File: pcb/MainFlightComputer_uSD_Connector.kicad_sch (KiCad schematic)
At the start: 10 parts, among them J5 0472192001

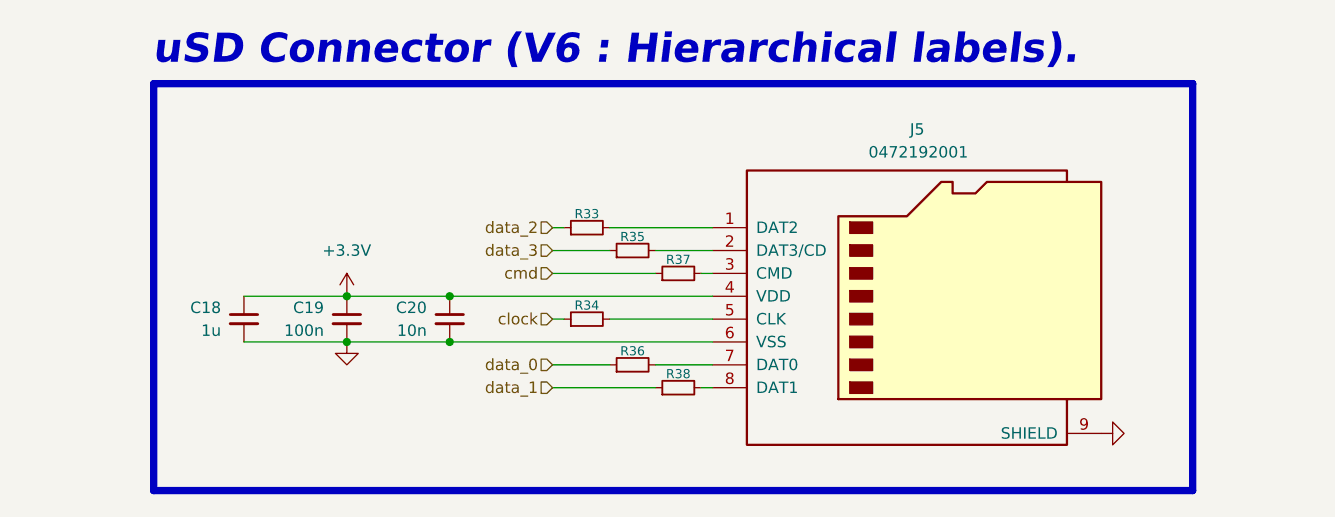
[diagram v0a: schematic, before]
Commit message: Updated design blocks in `MainFlightComputer`.
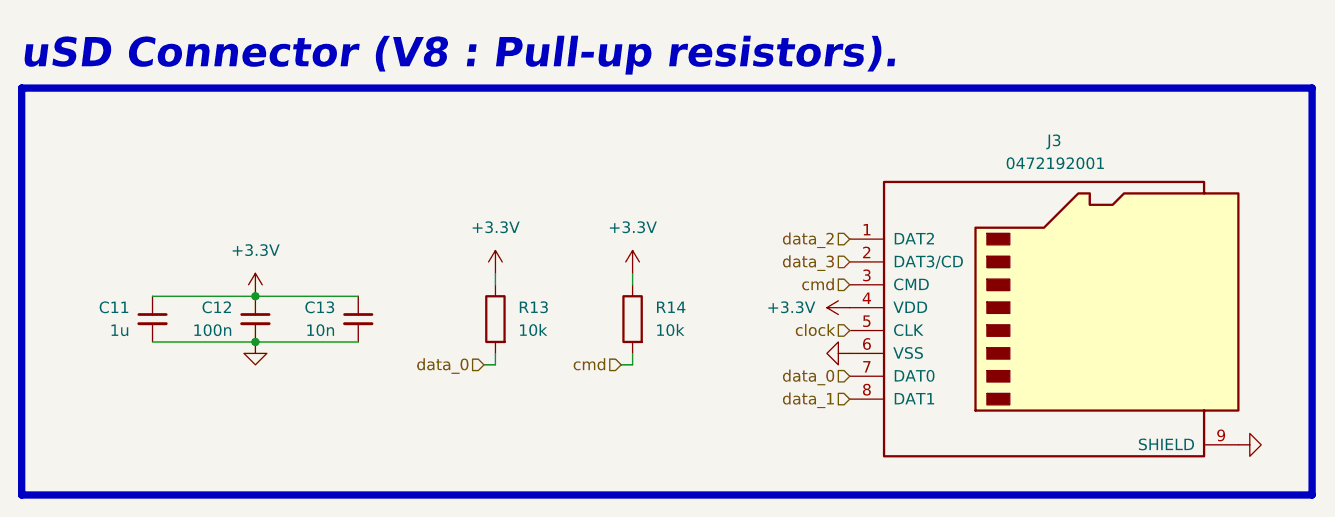
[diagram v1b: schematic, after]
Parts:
- removed R33, R34, R35, R36, R37, R38: R_Small, Resistor_SMD:R_1206_3216Metric_Pad1.30x1.75mm_HandSolder, symbol Device:R_Small
- added R13, R14: 10k, Resistor_SMD:R_1206_3216Metric_Pad1.30x1.75mm_HandSolder, symbol Device:R
- renumbered C18 to C11, C19 to C12, C20 to C13, J5 to J3
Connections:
- net +3.3V: now also R13.1, R14.1
- net clock: now also J3.5 (CLK)
- net cmd: now also J3.3 (CMD), R14.2
- net data_0: now also J3.7 (DAT0), R13.2
- net data_1: now also J3.8 (DAT1)
- net data_2: now also J3.1 (DAT2)
- net data_3: now also J3.2 (DAT3/CD)
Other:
- note added: "uSD Connector (V8 : Pull-up resistors)."
- note removed: "uSD Connector (V6 : Hierarchical labels)."
- moved on the sheet: C11, C12, C13, J3

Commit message: Laid out silkscreen for `MainFlightComputer`.
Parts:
- renumbered C13 to C17, C12 to C18, C11 to C19, J3 to J2, R13 to R14, R14 to R15
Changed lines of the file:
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@@
 		(on_board yes)
 		(dnp no)
-		(property "Reference" "R14"
+		(property "Reference" "R15"
 			(at 100.33 78.7399 0)
 			(effects
@@
 			(project ""
 				(path "/0a179c33-cb18-4019-99e7-0e00d41f97d6/d6d791b4-6a15-48a1-8b16-290665bcc58d"
-					(reference "R14")
+					(reference "R15")
 					(unit 1)
 				)
@@
 		(on_board yes)
 		(dnp no)
-		(property "Reference" "C11"
+		(property "Reference" "C19"
 			(at 41.91 78.7462 0)
 			(effects
@@
 			(project ""
 				(path "/0a179c33-cb18-4019-99e7-0e00d41f97d6/d6d791b4-6a15-48a1-8b16-290665bcc58d"
-					(reference "C11")
+					(reference "C19")
 					(unit 1)
 				)
@@
 		(on_board yes)
 		(dnp no)
-		(property "Reference" "C12"
+		(property "Reference" "C18"
 			(at 53.34 78.7462 0)
 			(effects
@@
 			(project ""
 				(path "/0a179c33-cb18-4019-99e7-0e00d41f97d6/d6d791b4-6a15-48a1-8b16-290665bcc58d"
-					(reference "C12")
+					(reference "C18")
 					(unit 1)
 				)
@@
 		(on_board yes)
 		(dnp no)
-		(property "Reference" "J3"
+		(property "Reference" "J2"
 			(at 144.653 60.198 0)
 			(effects
@@
 			(project ""
 				(path "/0a179c33-cb18-4019-99e7-0e00d41f97d6/d6d791b4-6a15-48a1-8b16-290665bcc58d"
-					(reference "J3")
+					(reference "J2")
 					(unit 1)
 				)
@@
 		(on_board yes)
 		(dnp no)
-		(property "Reference" "R13"
+		(property "Reference" "R14"
 			(at 85.09 78.7399 0)
 			(effects
@@
 			(project ""
 				(path "/0a179c33-cb18-4019-99e7-0e00d41f97d6/d6d791b4-6a15-48a1-8b16-290665bcc58d"
-					(reference "R13")
+					(reference "R14")
 					(unit 1)
 				)
@@
 		(on_board yes)
 		(dnp no)
-		(property "Reference" "C13"
+		(property "Reference" "C17"
 			(at 64.77 78.7462 0)
 			(effects
@@
 			(project ""
 				(path "/0a179c33-cb18-4019-99e7-0e00d41f97d6/d6d791b4-6a15-48a1-8b16-290665bcc58d"
-					(reference "C13")
-					(unit 1)
-				)
+					(reference "C17")
+					(unit 1)
+				)
